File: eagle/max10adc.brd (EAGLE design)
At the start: 98 x 62 mm, 156 parts, among them IC1 MAX19506, IC2 MAX19506, J1 MOLEX_BNC_73100-0105, J2 MOLEX_BNC_73100-0105, J3 MOLEX_BNC_73100-0105, J4 MOLEX_BNC_73100-0105, U1 MAX4416ESA, U2 MAX4416ESA, U340G CH340G, Y1 ABL-12.000MHZ-B2

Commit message: some more stuff
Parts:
- RLED1, RLED2, RLED3, RLED4: value 220 -> 560
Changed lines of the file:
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@@
 <attribute name="OC_NEWARK" value="unknown" x="9.42" y="57.03" size="1.778" layer="27" rot="R90" display="off"/>
 </element>
-<element name="RLED1" library="resistor" package="R0805" value="220" x="5.53" y="56.44" smashed="yes" rot="R180">
+<element name="RLED1" library="resistor" package="R0805" value="560" x="5.53" y="56.44" smashed="yes" rot="R180">
 <attribute name="MF" value="" x="5.53" y="56.44" size="1.778" layer="27" rot="R180" display="off"/>
-<attribute name="MPN" value="MF-RES-0805-220" x="5.53" y="56.44" size="1.778" layer="27" rot="R180" display="off"/>
+<attribute name="MPN" value="MF-RES-0805-560" x="5.53" y="56.44" size="1.778" layer="27" rot="R180" display="off"/>
 <attribute name="OC_NEWARK" value="unknown" x="5.53" y="56.44" size="1.778" layer="27" rot="R180" display="off"/>
 <attribute name="VALUE" x="4.5826" y="58.33" size="0.8128" layer="21" font="vector"/>
@@
 <attribute name="MPN" value="MF-CAP-0805-0.1uF" x="58.08" y="20.8" size="1.778" layer="27" display="off"/>
 </element>
-<element name="RLED2" library="resistor" package="R0805" value="220" x="5.52" y="53.44" smashed="yes" rot="R180">
+<element name="RLED2" library="resistor" package="R0805" value="560" x="5.52" y="53.44" smashed="yes" rot="R180">
 <attribute name="MF" value="" x="5.52" y="53.44" size="1.778" layer="27" rot="R180" display="off"/>
-<attribute name="MPN" value="MF-RES-0805-220" x="5.52" y="53.44" size="1.778" layer="27" rot="R180" display="off"/>
+<attribute name="MPN" value="MF-RES-0805-560" x="5.52" y="53.44" size="1.778" layer="27" rot="R180" display="off"/>
 <attribute name="OC_NEWARK" value="unknown" x="5.52" y="53.44" size="1.778" layer="27" rot="R180" display="off"/>
 </element>
@@
 <attribute name="OC_NEWARK" value="unknown" x="11.52" y="57.02" size="1.778" layer="27" rot="R90" display="off"/>
 </element>
-<element name="RLED3" library="resistor" package="R0805" value="220" x="5.51" y="50.64" smashed="yes" rot="R180">
+<element name="RLED3" library="resistor" package="R0805" value="560" x="5.51" y="50.64" smashed="yes" rot="R180">
 <attribute name="MF" value="" x="5.51" y="50.64" size="1.778" layer="27" rot="R180" display="off"/>
-<attribute name="MPN" value="MF-RES-0805-220" x="5.51" y="50.64" size="1.778" layer="27" rot="R180" display="off"/>
+<attribute name="MPN" value="MF-RES-0805-560" x="5.51" y="50.64" size="1.778" layer="27" rot="R180" display="off"/>
 <attribute name="OC_NEWARK" value="unknown" x="5.51" y="50.64" size="1.778" layer="27" rot="R180" display="off"/>
 </element>
@@
 <attribute name="NAME" x="29.135" y="52" size="0.3048" layer="33" ratio="10" rot="R180"/>
 </element>
-<element name="RLED4" library="resistor" package="R0805" value="220" x="5.5" y="47.8" smashed="yes" rot="R180">
+<element name="RLED4" library="resistor" package="R0805" value="560" x="5.5" y="47.8" smashed="yes" rot="R180">
 <attribute name="MF" value="" x="5.5" y="47.8" size="1.778" layer="27" rot="R180" display="off"/>
-<attribute name="MPN" value="MF-RES-0805-220" x="5.5" y="47.8" size="1.778" layer="27" rot="R180" display="off"/>
+<attribute name="MPN" value="MF-RES-0805-560" x="5.5" y="47.8" size="1.778" layer="27" rot="R180" display="off"/>
 <attribute name="OC_NEWARK" value="unknown" x="5.5" y="47.8" size="1.778" layer="27" rot="R180" display="off"/>
 </element>

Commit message: some more stuff
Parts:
- removed AC_SW1, AC_SW2, AC_SW3, AC_SW4: 741G3157DBVR, 74xx-little-us@1:DBV_R-PDSO-G6
- added ACR1, ACR2, ACR3, ACR4: 560, resistor:R0805
- added K1, K2, K3, K4: AQY21SOP, relay:SOP04
- moved C_AC2 0.40 mm to (75.0, 14.0), turned to 180 degrees
- moved C_AC3 0.40 mm to (75.0, 44.0)
- moved C_AC4 0.20 mm to (75.0, 47.0), turned to 180 degrees
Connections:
- removed net N$14: AC_SW1.3, C_AC1.2
- removed net N$17: AC_SW2.1, CIN2.1, C_AC2.1, RIN2.1
- removed net N$20: AC_SW3.1, CIN3.1, C_AC3.1, RIN3.1
- removed net N$22: AC_SW4.1, CIN4.1, C_AC4.1, RIN4.1
- new net N$10: CIN1.1, C_AC1.1, K1.4, RIN1.1
- new net N$11: ACR1.2, K1.1
- new net N$32: ACR3.2, K3.1
- new net N$35: ACR4.2, K4.1
- net +3V3: no longer AC_SW1.5, AC_SW2.5, AC_SW3.5, AC_SW4.5
- net E_ACSW1: now also ACR1.1; no longer AC_SW1.6
- net E_ACSW2: now also ACR2.1; no longer AC_SW2.6
- net E_ACSW3: now also ACR3.1; no longer AC_SW3.6
- net E_ACSW4: now also ACR4.1; no longer AC_SW4.6
- net GND: now also K1.2, K2.2, K3.2, K4.2; no longer AC_SW1.2, AC_SW2.2, AC_SW3.2, AC_SW4.2
- net INJ1: now also C_AC1.2, K1.3; no longer AC_SW1.4
- net INJ2: now also C_AC2.2, K2.3; no longer AC_SW2.4
- net INJ3: now also C_AC3.2, K3.3; no longer AC_SW3.4
- net INJ4: now also C_AC4.2, K4.3; no longer AC_SW4.4
- net N$15: now also CIN2.1, C_AC2.1, K2.4, RIN2.1; no longer AC_SW1.1, CIN1.1, C_AC1.1, RIN1.1
- net N$16: now also CIN3.1, C_AC3.1, K3.4, RIN3.1; no longer AC_SW2.3, C_AC2.2
- net N$19: now also CIN4.1, C_AC4.1, K4.4, RIN4.1; no longer AC_SW3.3, C_AC3.2
- net N$21: now also ACR2.2, K2.1; no longer AC_SW4.3, C_AC4.2
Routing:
- net +3V3: track 530.1 -> 0.00 mm
- net +5V: track 257.8 -> 0.00 mm
- net GND: track 178.9 -> 0.00 mm, vias 87 -> 0
- net E_ACSW3: track 128.0 -> 0.00 mm, vias 2 -> 0
- net E_GSW3: track 123.9 -> 0.00 mm, vias 2 -> 0
- net E_ACSW4: track 123.3 -> 0.00 mm, vias 2 -> 0
- net E_OVSAMP1: track 120.8 -> 0.00 mm, vias 2 -> 0
- net E_GSW4: track 117.9 -> 0.00 mm, vias 3 -> 0
- net E_OVSAMP2: track 113.9 -> 0.00 mm, vias 3 -> 0
- net L141_SCL: track 105.2 -> 0.00 mm, vias 5 -> 0
- net L21_SDA: track 104.6 -> 0.00 mm, vias 6 -> 0
- net E_ACSW2: track 97.0 -> 0.00 mm, vias 2 -> 0
- net E_SHDN: track 91.9 -> 0.00 mm, vias 5 -> 0
- net E_ACSW1: track 88.2 -> 0.00 mm, vias 3 -> 0
- net E_GSW2: track 86.9 -> 0.00 mm, vias 2 -> 0
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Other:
- board text added: "Max10 ADC v8.6"
- board text removed: "Max10 ADC v8.5"

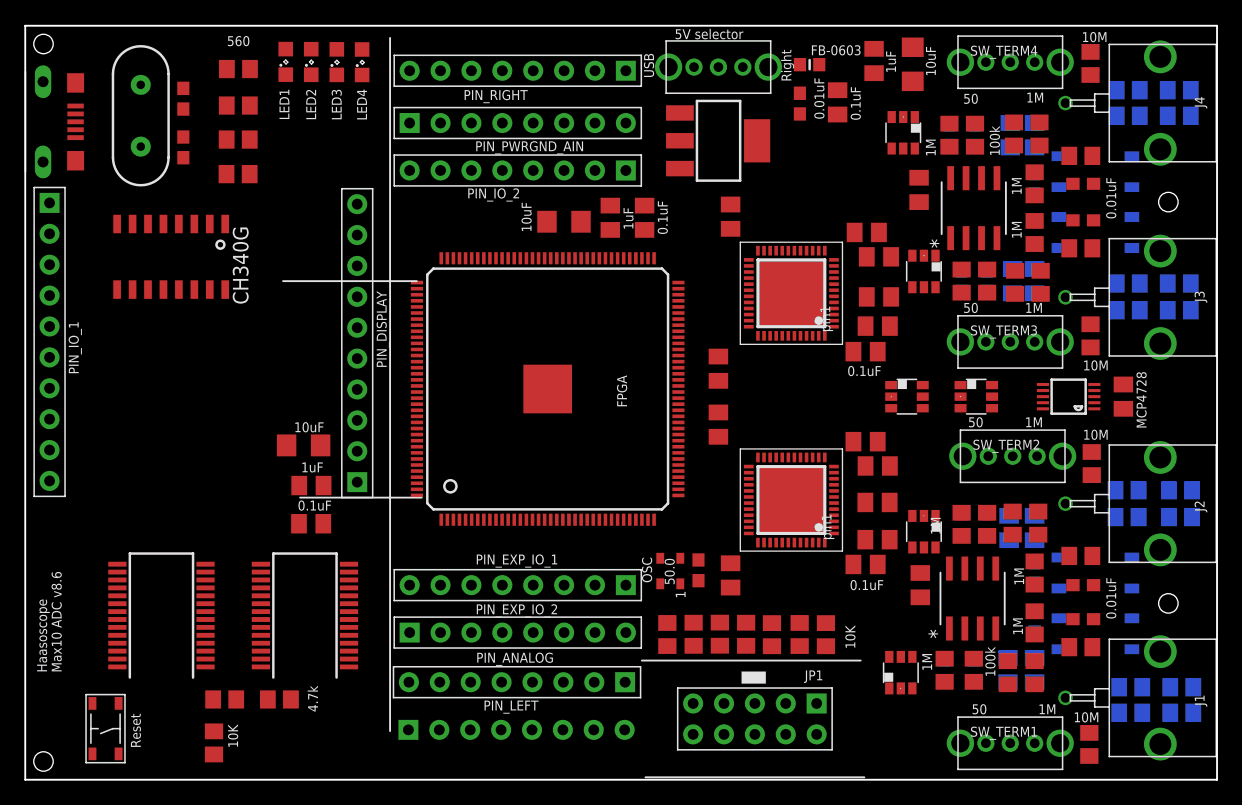
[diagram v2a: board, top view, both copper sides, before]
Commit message: routing of 8.6
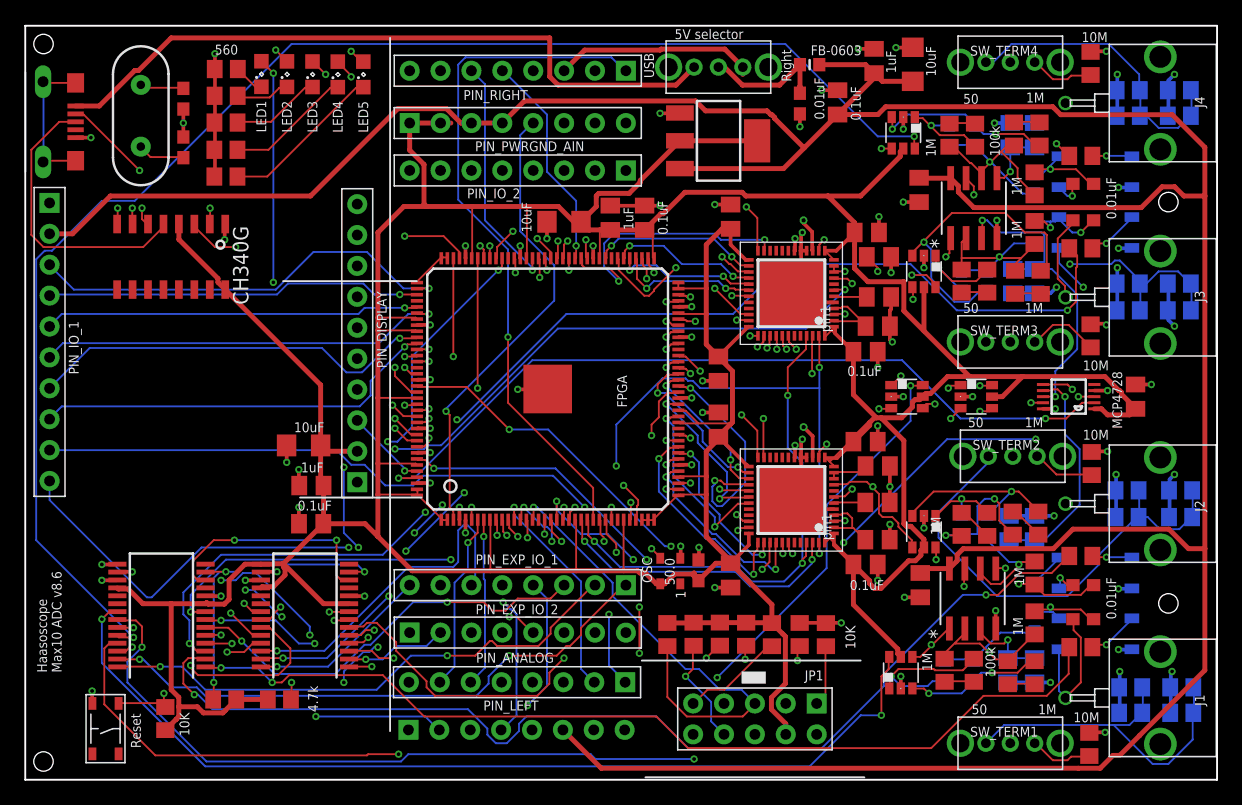
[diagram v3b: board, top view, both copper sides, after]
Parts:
- added LED5: MF-LED-0805-RED, led:SML0805
- added RLED5: 560, resistor:R0805
- moved RS9 4.47 mm to (-0.48, 3.03)
- moved LED1 2.24 mm to (7.42, 56.0)
- moved LED2 2.24 mm to (9.52, 56.0)
- moved LED3 2.24 mm to (11.6, 56.0)
- moved LED4 2.24 mm to (13.7, 56.0)
- moved RLED4 2.24 mm to (4.50, 49.8)
- moved RLED3 1.72 mm to (4.51, 52.0)
- moved RLED2 1.28 mm to (4.52, 54.2)
- moved COFFSET 1.00 mm to (79.3, 29.5)
- moved RLED1 1.00 mm to (4.53, 56.4)
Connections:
- removed net LEDBASE: IOEXPAND_0X24_TOP.25, RLED1.2, RLED2.2, RLED3.2, RLED4.2
- removed net N$34: LED1.A, RLED1.1
- removed net N$95: LED2.A, RLED2.1
- removed net N$97: LED3.A, RLED3.1
- new net LED5: IOEXPAND_0X24_TOP.25, LED5.A
- new net N$12: LED3.C, RLED3.1
- new net N$13: LED2.C, RLED2.1
- new net N$14: LED1.C, RLED1.1
- new net N$17: LED5.C, RLED5.1
- net GND: now also RLED1.2, RLED2.2, RLED3.2, RLED4.2, RLED5.2
- net LED1: now also LED1.A; no longer LED1.C
- net LED2: now also LED2.A; no longer LED2.C
- net LED3: now also LED3.A; no longer LED3.C
- net LED4: now also LED4.A; no longer LED4.C
- net N$1: now also LED4.C; no longer LED4.A
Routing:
- net +3V3: track 0.00 -> 488.4 mm
- net +5V: track 0.00 -> 281.1 mm
- net GND: track 0.00 -> 174.1 mm, vias 0 -> 89
- net E_ACSW4: track 0.00 -> 148.2 mm, vias 0 -> 2
- net E_OVSAMP2: track 0.00 -> 134.5 mm, vias 0 -> 2
- net E_GSW4: track 0.00 -> 119.6 mm, vias 0 -> 2
- net E_GSW3: track 0.00 -> 113.8 mm, vias 0 -> 2
- net L141_SCL: track 0.00 -> 106.2 mm, vias 0 -> 5
- net E_ACSW3: track 0.00 -> 101.0 mm, vias 0 -> 4
- net L21_SDA: track 0.00 -> 98.9 mm, vias 0 -> 7
- net E_OVSAMP1: track 0.00 -> 93.2 mm, vias 0 -> 3
- net E_GSW2: track 0.00 -> 90.0 mm, vias 0 -> 3
- net LED2: track 0.00 -> 88.4 mm, vias 0 -> 2
- net E_ACSW2: track 0.00 -> 88.4 mm, vias 0 -> 2
- net E_SHDN: track 0.00 -> 87.6 mm, vias 0 -> 4
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
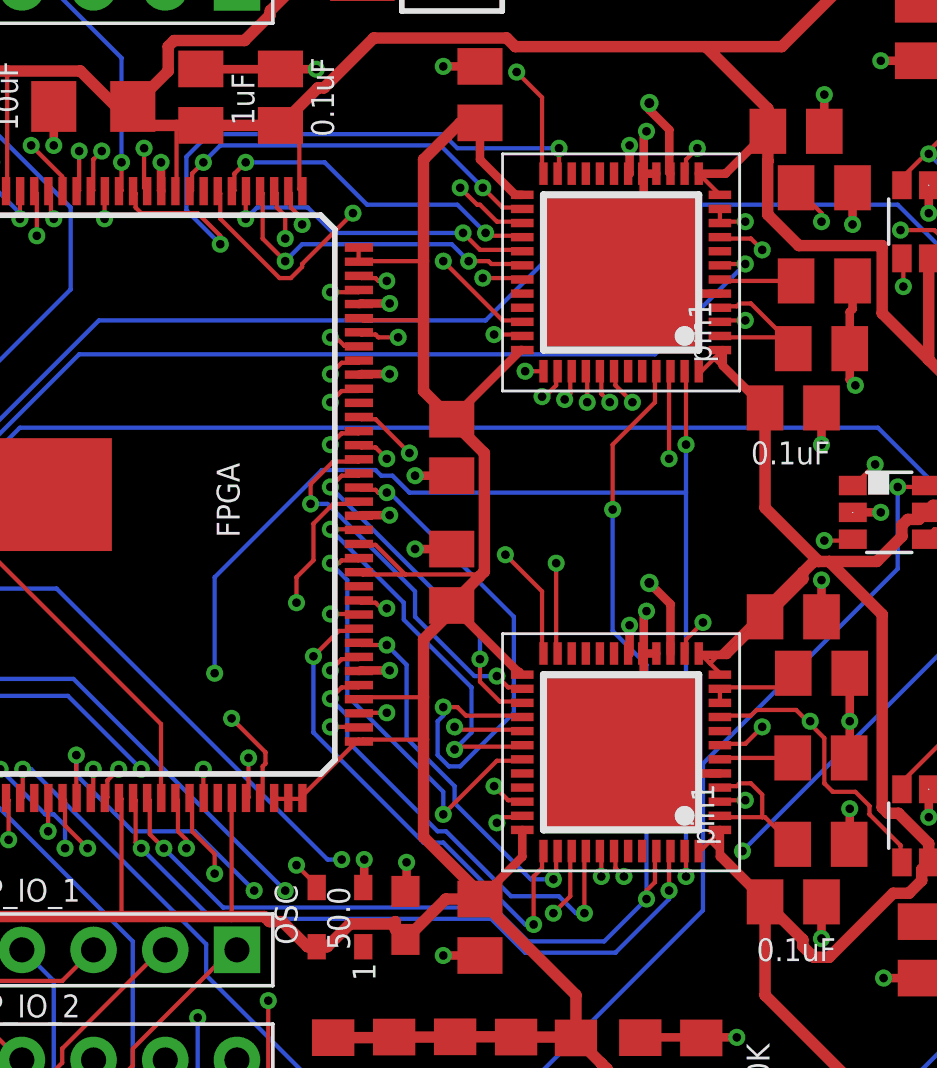
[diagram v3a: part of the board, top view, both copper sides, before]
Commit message: routing of 8.6
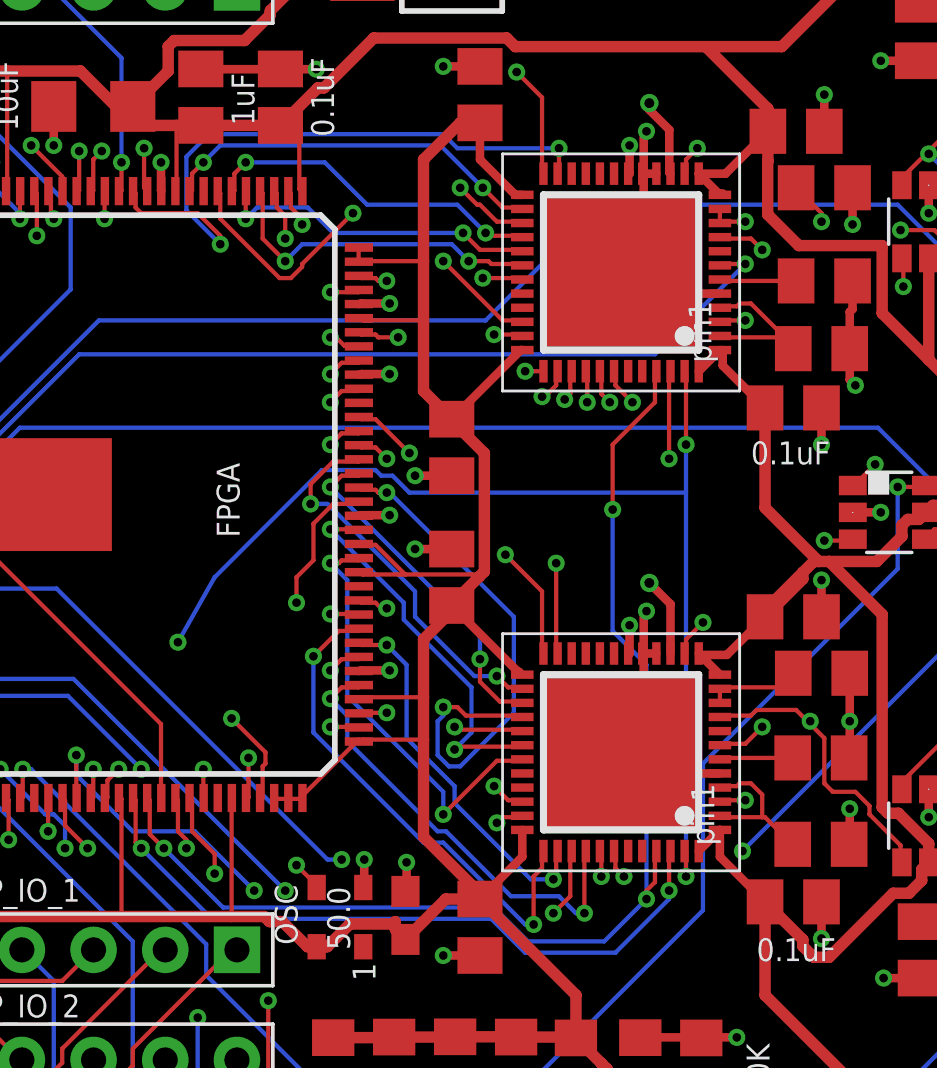
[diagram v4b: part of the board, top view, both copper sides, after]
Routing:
- net +3V3: track 488.4 -> 484.0 mm
- net LOW_22: track 47.0 -> 46.4 mm
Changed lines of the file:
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@@
 <layers>
 <layer number="1" name="Top" color="4" fill="1" visible="yes" active="yes"/>
-<layer number="2" name="Route2" color="1" fill="3" visible="yes" active="yes"/>
+<layer number="2" name="Route2" color="58" fill="10" visible="no" active="yes"/>
 <layer number="3" name="Route3" color="4" fill="3" visible="no" active="no"/>
 <layer number="4" name="Route4" color="1" fill="4" visible="no" active="no"/>
@@
 <layer number="13" name="Route13" color="4" fill="5" visible="no" active="no"/>
 <layer number="14" name="Route14" color="1" fill="6" visible="no" active="no"/>
-<layer number="15" name="Route15" color="4" fill="6" visible="yes" active="yes"/>
+<layer number="15" name="Route15" color="13" fill="1" visible="yes" active="yes"/>
 <layer number="16" name="Bottom" color="1" fill="1" visible="yes" active="yes"/>
 <layer number="17" name="Pads" color="2" fill="1" visible="yes" active="yes"/>
@@
 <wire x1="39.6" y1="19.35" x2="39.71" y2="19.38" width="0.1524" layer="1"/>
 <wire x1="39.3" y1="19.35" x2="39.21" y2="19.38" width="0.1524" layer="1"/>
-<wire x1="53.75" y1="41.5" x2="54.5" y2="40.75" width="0.1524" layer="1"/>
-<wire x1="54.6" y1="35.25" x2="54.3" y2="34.95" width="0.1524" layer="1"/>
-<wire x1="54.3" y1="34.95" x2="53.85" y2="34.5" width="0.1524" layer="1"/>
-<wire x1="53.85" y1="34.5" x2="53.75" y2="34.5" width="0.1524" layer="1"/>
+<wire x1="54.5" y1="40.75" x2="53.75" y2="41.5" width="0.1524" layer="1"/>
+<wire x1="54.6" y1="35.25" x2="53.85" y2="34.5" width="0.1524" layer="1"/>
+<wire x1="53.75" y1="34.5" x2="53.85" y2="34.5" width="0.1524" layer="1"/>
 <wire x1="54.6" y1="35.25" x2="54.5" y2="35.25" width="0.1524" layer="1"/>
-<wire x1="53.85" y1="24.45" x2="54.15" y2="24.15" width="0.1524" layer="1"/>
-<wire x1="54.15" y1="24.15" x2="54.45" y2="23.85" width="0.1524" layer="1"/>
-<wire x1="54.45" y1="23.85" x2="54.5" y2="23.75" width="0.1524" layer="1"/>
+<wire x1="53.85" y1="24.45" x2="54.45" y2="23.85" width="0.1524" layer="1"/>
+<wire x1="54.5" y1="23.75" x2="54.45" y2="23.85" width="0.1524" layer="1"/>
 <wire x1="53.85" y1="24.45" x2="53.75" y2="24.5" width="0.1524" layer="1"/>
-<wire x1="54.45" y1="18.15" x2="54.15" y2="17.85" width="0.1524" layer="1"/>
-<wire x1="54.15" y1="17.85" x2="53.85" y2="17.55" width="0.1524" layer="1"/>
-<wire x1="53.85" y1="17.55" x2="53.75" y2="17.5" width="0.1524" layer="1"/>
-<wire x1="54.5" y1="18.25" x2="54.45" y2="18.15" width="0.1524" layer="1"/>
 <wire x1="41.7" y1="38.85" x2="41.7" y2="38.4" width="0.1524" layer="1"/>
 <wire x1="41.7" y1="38.4" x2="41.71" y2="38.38" width="0.1524" layer="1"/>
@@
 <wire x1="44" y1="38.4" x2="41.85" y2="38.4" width="0.1524" layer="1"/>
 <wire x1="41.85" y1="38.4" x2="41.71" y2="38.38" width="0.1524" layer="1"/>
-<wire x1="56.1" y1="15.9" x2="54.15" y2="17.85" width="0.1524" layer="1"/>
 <wire x1="56.1" y1="15.9" x2="56.1" y2="15.7" width="0.1524" layer="1"/>
-<wire x1="55.95" y1="25.95" x2="54.15" y2="24.15" width="0.1524" layer="1"/>
 <wire x1="55.95" y1="25.95" x2="56.1" y2="25.8" width="0.1524" layer="1"/>
-<wire x1="55.95" y1="33.3" x2="54.3" y2="34.95" width="0.1524" layer="1"/>
 <wire x1="55.95" y1="33.3" x2="56.1" y2="33.2" width="0.1524" layer="1"/>
 <wire x1="54.6" y1="40.8" x2="54.5" y2="40.75" width="0.1524" layer="1"/>
@@
 <wire x1="46" y1="42" x2="47.25" y2="40.75" width="0.3048" layer="1"/>
 <wire x1="47.25" y1="40.75" x2="47.5" y2="40.75" width="0.3048" layer="1"/>
+<wire x1="54.5" y1="18.25" x2="53.75" y2="17.5" width="0.3048" layer="1"/>
+<wire x1="53.75" y1="24.5" x2="54.5" y2="23.75" width="0.3048" layer="1"/>
+<wire x1="54.5" y1="35.25" x2="53.75" y2="34.5" width="0.3048" layer="1"/>
+<wire x1="53.75" y1="41.5" x2="54.45" y2="40.8" width="0.3048" layer="1"/>
+<wire x1="54.45" y1="40.8" x2="54.6" y2="40.8" width="0.3048" layer="1"/>
 </signal>
 <signal name="TCK">
@@
 <wire x1="52" y1="44" x2="43" y2="44" width="0.3048" layer="15"/>
 <wire x1="43" y1="44" x2="37" y2="38" width="0.3048" layer="15"/>
-<wire x1="37" y1="38" x2="37" y2="34" width="0.3048" layer="15"/>
 <wire x1="38.3" y1="20.5" x2="38.3" y2="19.4" width="0.1524" layer="1"/>
 <wire x1="38.4" y1="20.6" x2="38.3" y2="20.5" width="0.1524" layer="1"/>
 <wire x1="38.4" y1="21" x2="38.4" y2="20.6" width="0.1524" layer="1"/>
 <wire x1="37.2" y1="22.2" x2="38.4" y2="21" width="0.1524" layer="1"/>
-<wire x1="37.2" y1="33.8" x2="37.2" y2="22.2" width="0.1524" layer="15"/>
 <wire x1="38.3" y1="19.4" x2="38.21" y2="19.38" width="0.1524" layer="1"/>
-<wire x1="37.2" y1="33.8" x2="37" y2="34" width="0.1524" layer="15"/>
 <via x="37.2" y="22.2" extent="1-16" drill="0.3048"/>
+<wire x1="37" y1="22.4" x2="37.2" y2="22.2" width="0.3048" layer="15"/>
+<wire x1="37" y1="38" x2="37" y2="22.4" width="0.3048" layer="15"/>
 </signal>
 <signal name="D1C">
@@
 <wire x1="32.8" y1="20" x2="32.8" y2="19.4" width="0.1524" layer="1"/>
 <wire x1="33.2" y1="20.4" x2="32.8" y2="20" width="0.1524" layer="1"/>
-<wire x1="36.6" y1="23.8" x2="33.2" y2="20.4" width="0.1524" layer="15"/>
-<wire x1="36.6" y1="27.2" x2="36.6" y2="23.8" width="0.1524" layer="16"/>
+<wire x1="35.3" y1="24.9" x2="33.2" y2="20.4" width="0.1524" layer="15"/>
+<wire x1="36.6" y1="27.2" x2="35.3" y2="24.9" width="0.1524" layer="16"/>
 <wire x1="40.4" y1="31" x2="36.6" y2="27.2" width="0.1524" layer="16"/>
 <wire x1="42.3" y1="31" x2="40.4" y2="31" width="0.1524" layer="16"/>
@@
 <via x="53.3" y="31.9" extent="1-16" drill="0.3048"/>
 <via x="33.2" y="20.4" extent="1-16" drill="0.3048"/>
-<via x="36.6" y="23.8" extent="1-16" drill="0.3048"/>
+<via x="35.3" y="24.9" extent="1-16" drill="0.3048"/>
 </signal>
 <signal name="L134">
@@
 <wire x1="39" y1="27" x2="38" y2="26" width="0.3048" layer="15"/>
 <wire x1="37.8" y1="20.8" x2="37.8" y2="19.4" width="0.1524" layer="1"/>
-<wire x1="37.8" y1="25.8" x2="37.8" y2="20.8" width="0.1524" layer="15"/>
 <wire x1="37.8" y1="19.4" x2="37.71" y2="19.38" width="0.1524" layer="1"/>
-<wire x1="37.8" y1="25.8" x2="38" y2="26" width="0.1524" layer="15"/>
 <via x="37.8" y="20.8" extent="1-16" drill="0.3048"/>
+<wire x1="38" y1="26" x2="38" y2="21" width="0.3048" layer="15"/>
+<wire x1="38" y1="21" x2="37.8" y2="20.8" width="0.3048" layer="15"/>
 </signal>
 <signal name="IO_101">

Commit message: for board 8
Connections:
- net L128 renamed L127
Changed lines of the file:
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@@
 <via x="21.2" y="28.5" extent="1-16" drill="0.3048"/>
 </signal>
-<signal name="L128">
+<signal name="L127">
 <contactref element="FPGA" pad="127"/>
 <contactref element="PIN_DISPLAY" pad="9"/>
